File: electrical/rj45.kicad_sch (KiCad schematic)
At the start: 24 parts, among them J1 0826-1G1T-23-F, J2 0826-1G1T-23-F, J3 0826-1G1T-23-F

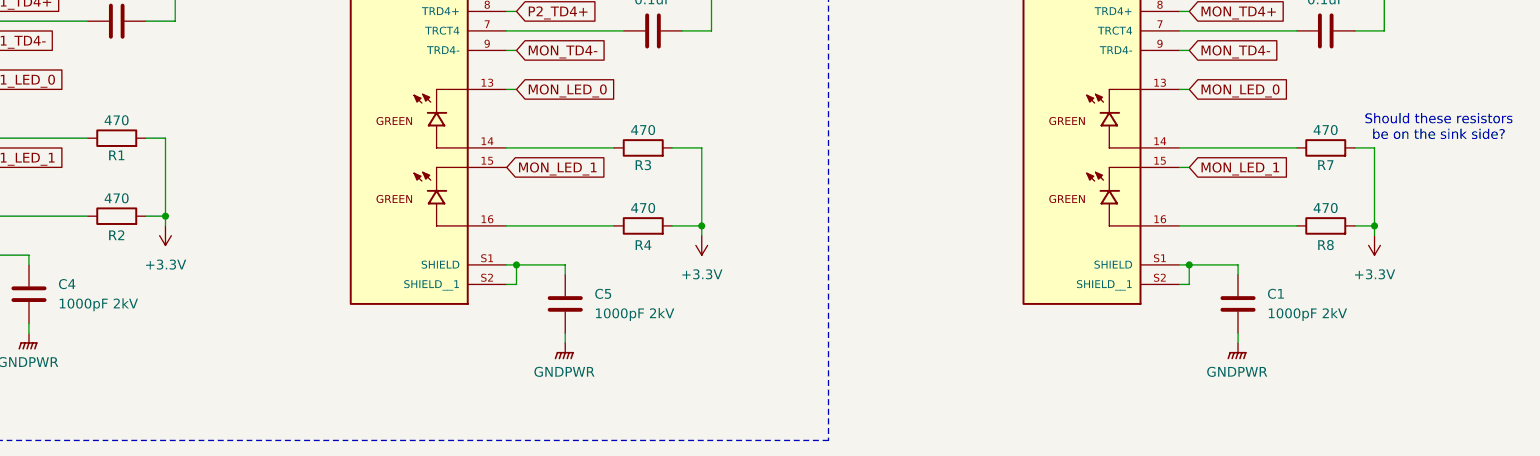
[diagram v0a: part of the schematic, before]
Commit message: Add Pi LEDs + center tap connections
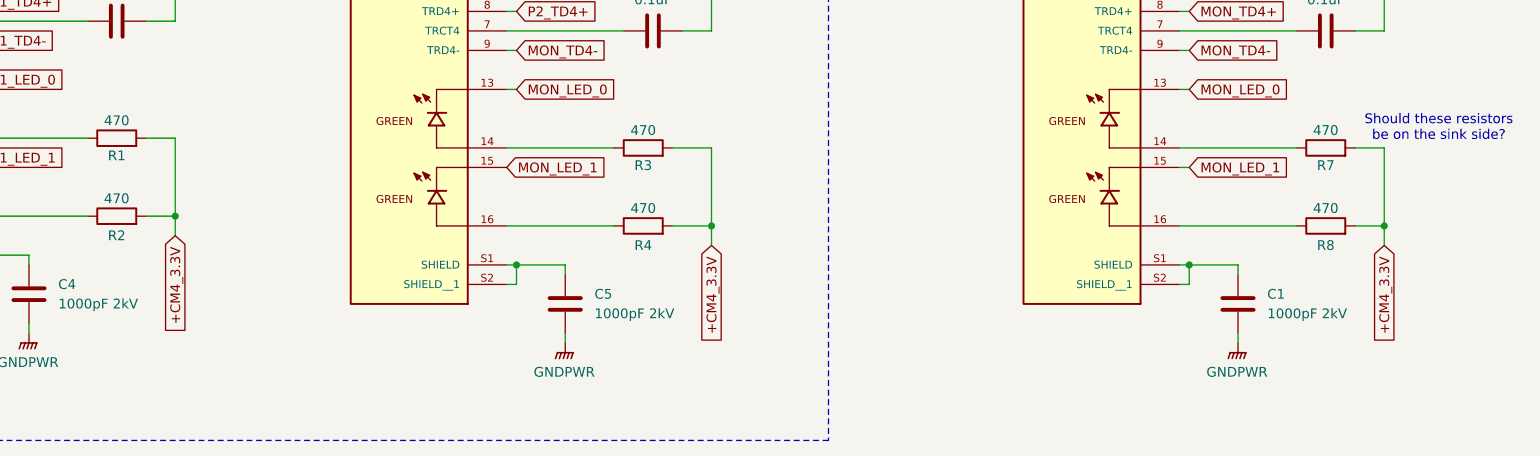
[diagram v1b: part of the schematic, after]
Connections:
- net +3.3V renamed +CM4_3.3V

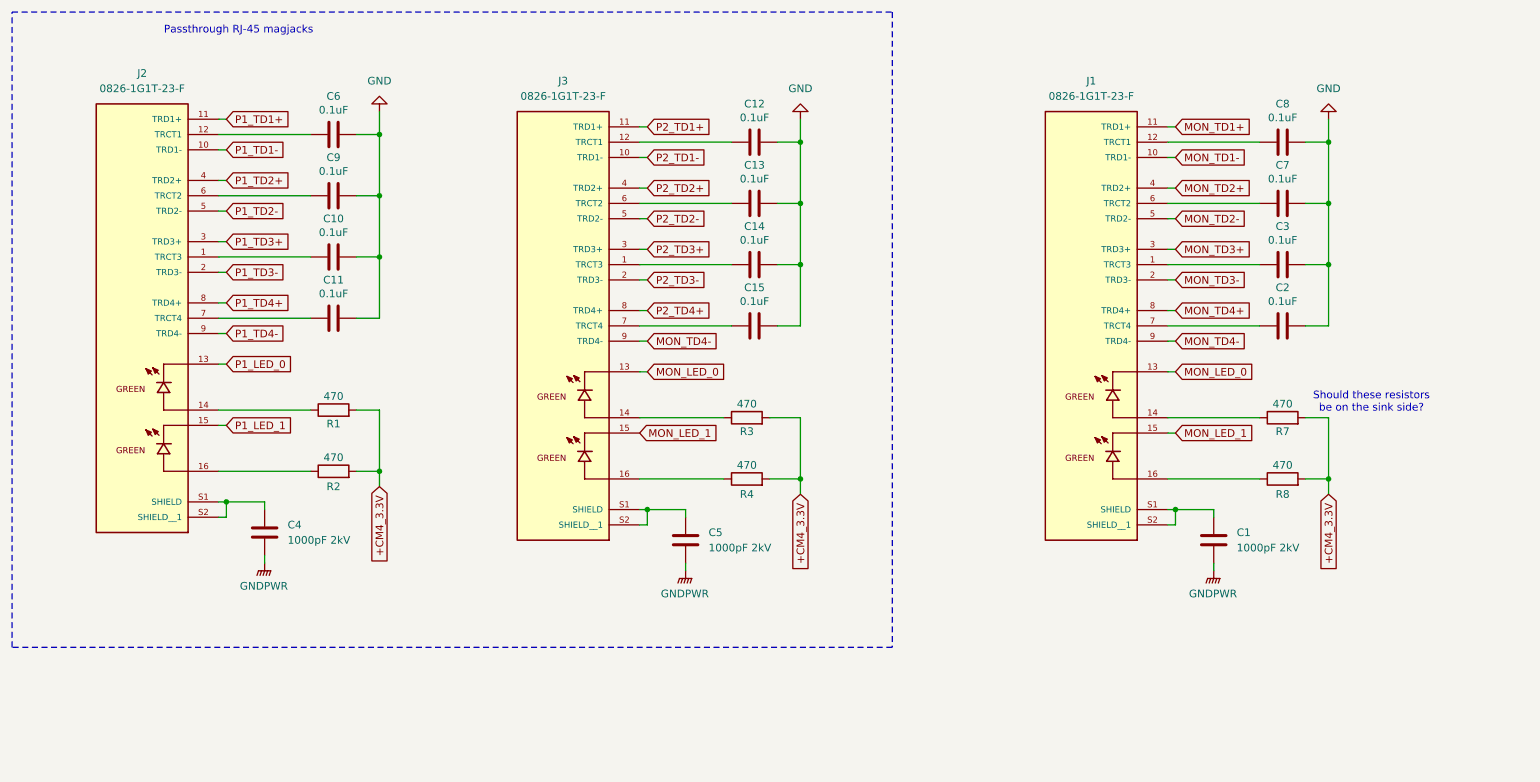
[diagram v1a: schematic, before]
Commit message: Pi <-> Switch SPI interface
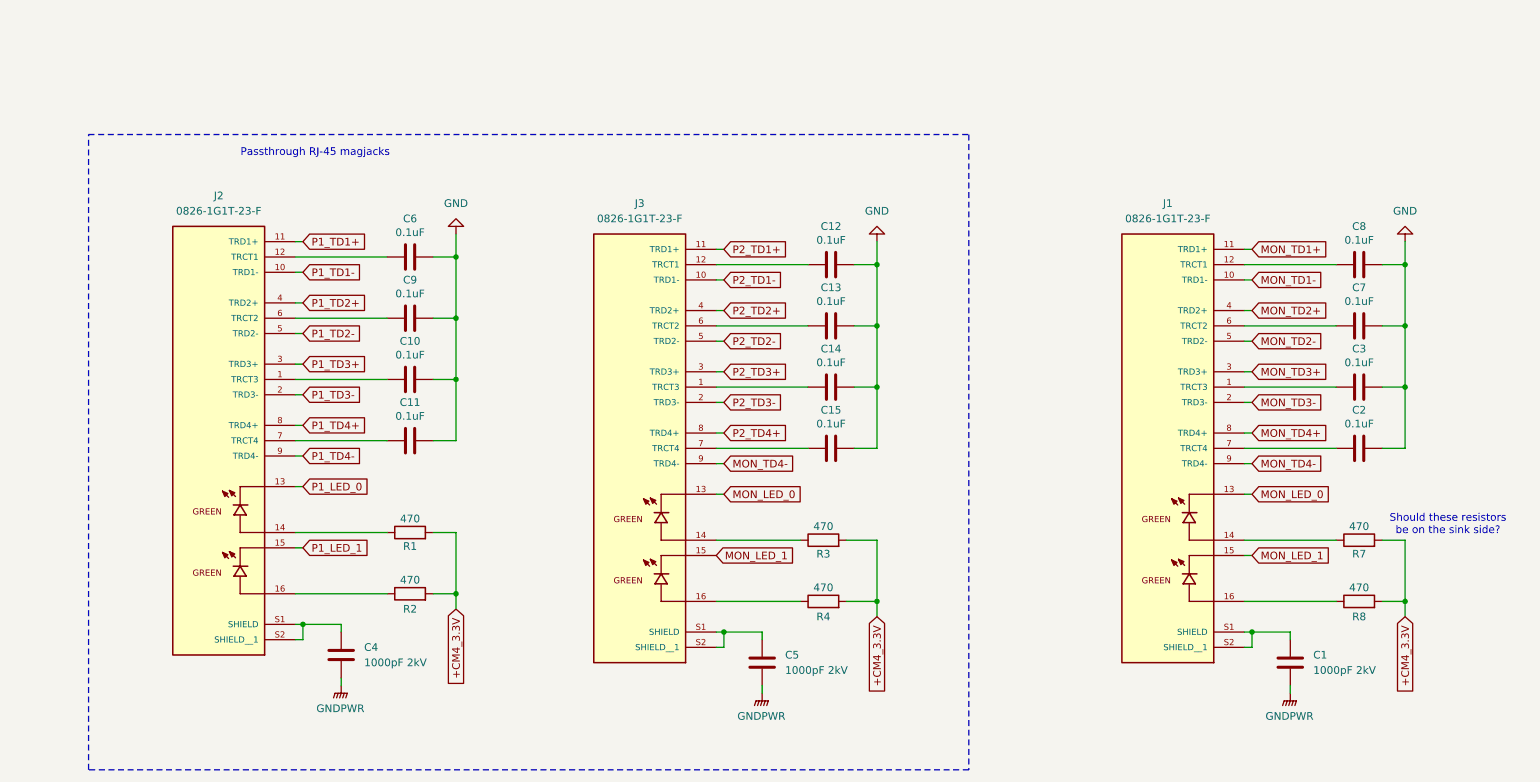
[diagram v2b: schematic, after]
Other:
- moved on the sheet: C1, C10, C11, C12, C13, C14, C15, C2, C3, C4, C5, C6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

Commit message: Micro B + Header for eMMC flash
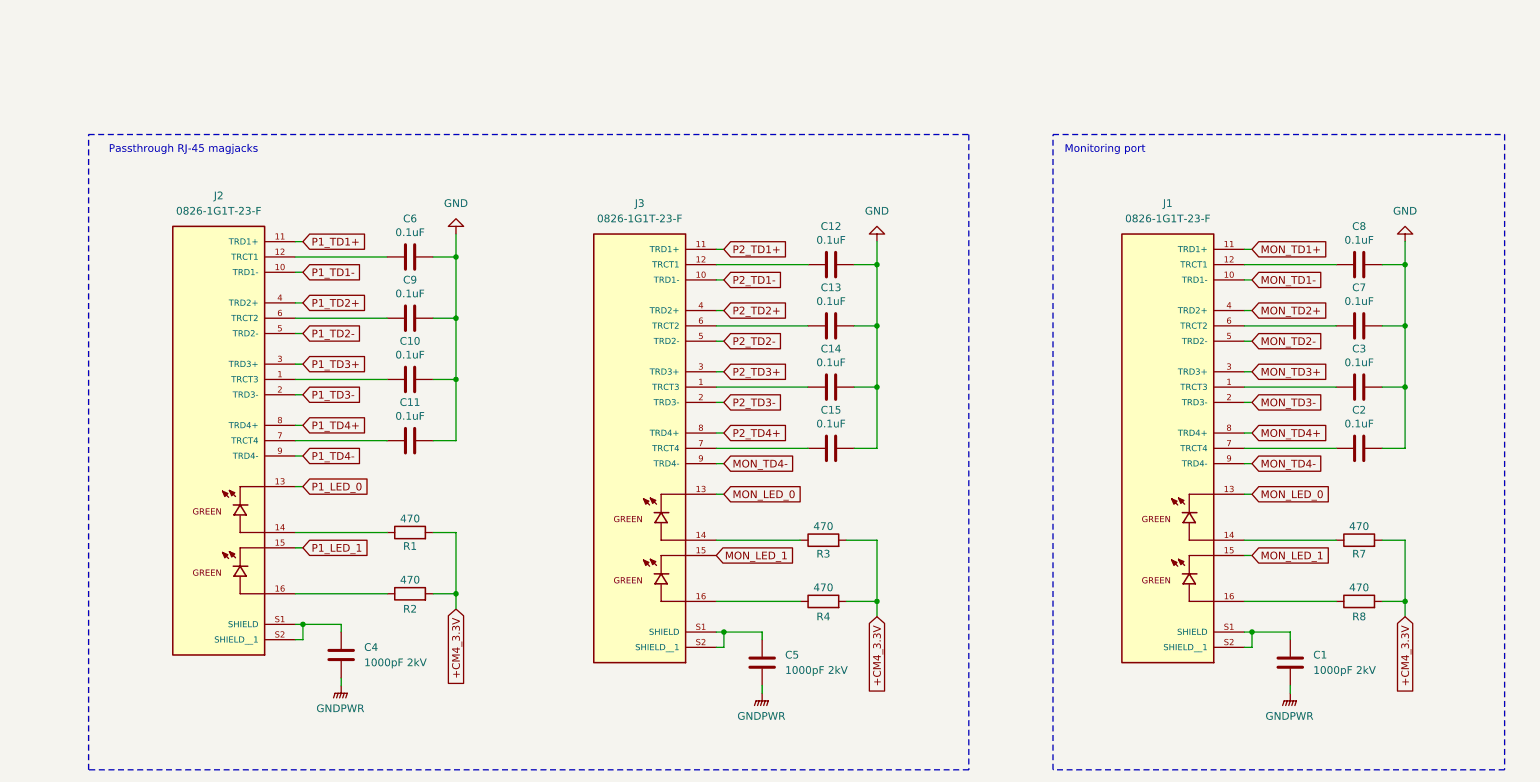
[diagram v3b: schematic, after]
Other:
- note added: "Monitoring port"
- note removed: "Should these resistors be on the sink side?"
- title: (none) -> Network Tap
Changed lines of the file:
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@@
 	(generator_version "8.0")
 	(paper "A4")
+	(title_block
+		(title "Network Tap")
+	)
 	(junction
 		(at 71.12 121.92)
@@
 			(width 0)
 			(type default)
+		)
+	)
+	(rectangle
+		(start 195.58 40.64)
+		(end 270.51 146.05)
+		(stroke
+			(width 0)
+			(type dash)
+		)
+		(fill
+			(type none)
 		)
 	)
@@
 	(text "Passthrough RJ-45 magjacks"
 		(exclude_from_sim no)
-		(at 73.152 43.688 0)
+		(at 51.308 43.18 0)
 		(effects
 			(font
@@
 		)
 	)
-	(text "Should these resistors \nbe on the sink side?"
+	(text "Monitoring port"
 		(exclude_from_sim no)
-		(at 261.112 105.41 0)
+		(at 204.216 43.18 0)
 		(effects
 			(font
